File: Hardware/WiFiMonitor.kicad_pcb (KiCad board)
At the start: 2 copper layers, 0 parts

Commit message: Final
Corregi nombres, y agregue el circuito de programación
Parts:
- added BTRTC1: 3.3V, Battery_Holders:Keystone_1058_1x2032-CoinCell, F.Cu at (120.9, 68.8)
- added C1: 2.2u, Capacitors_SMD:C_0603, F.Cu at (111.8, 99.3)
- added C2: 10u, Capacitors_SMD:C_0603, F.Cu at (112.5, 106.6)
- added C3: 4.7u, Capacitors_SMD:C_0603, F.Cu at (103.6, 94.0)
- added COMUN1: NC, PADS:PAD_5x3mm, F.Cu at (150.9, 90.6)
- added COMUN2: TORRETA, PADS:PAD_5x3mm, F.Cu at (142.6, 90.5)
- added D1: LED_ON, LEDs:LED_0603, F.Cu at (103.9, 100.9)
- added D2: LED_CHAR, LEDs:LED_0603, F.Cu at (103.6, 107.7)
- added D3: RB161, Diodes_SMD:D_SOD-123, F.Cu at (122.1, 112.5)
- added D4: RB161, Diodes_SMD:D_SOD-123, F.Cu at (128.9, 87.0)
- added IN1: 0_IN, PADS:PAD_5x3mm, F.Cu at (151.1, 102.9)
- added IN2: 1_IN, PADS:PAD_5x3mm, F.Cu at (142.5, 102.6)
- added IN3: 2_IN, PADS:PAD_5x3mm, F.Cu at (141.1, 96.2)
- added IN4: 3_IN, PADS:PAD_5x3mm, F.Cu at (154.3, 97.0)
- added J3: BATT, Connectors:PINHEAD1-2, F.Cu at (134.0, 112.0)
- added J4: ADAP_ESP, Pin_Headers:Pin_Header_Straight_2x08_Pitch2.54mm, F.Cu at (133.5, 87.0)
- added J5: FTDI, Pin_Headers:Pin_Header_Straight_1x05_Pitch2.54mm, F.Cu at (127.1, 102.5)
- added R1: 2K, Resistors_SMD:R_0603, F.Cu at (114.9, 91.3)
- added R10: 10K, Resistors_SMD:R_0603, F.Cu at (96.4, 106.8)
- added R11: 4.7K, Resistors_SMD:R_0603, F.Cu at (96.9, 112.3)
- added R12: 10K, Resistors_SMD:R_0603, F.Cu at (112.5, 112.5)
- added R13: 4.7K, Resistors_SMD:R_0603, F.Cu at (92.3, 86.4)
- added R14: 10K, Resistors_SMD:R_0603, F.Cu at (91.9, 91.4)
- added R15: 1K, Resistors_SMD:R_0603, F.Cu at (91.6, 96.1)
- added R16: 10K, Resistors_SMD:R_0603, F.Cu at (90.8, 100.7)
- added R17: 1K, Resistors_SMD:R_0603, F.Cu at (90.9, 106.1)
- added R18: 10K, Resistors_SMD:R_0603, F.Cu at (88.4, 112.3)
- added R2: 2K, Resistors_SMD:R_0603, F.Cu at (103.1, 112.8)
- added R3: 2K, Resistors_SMD:R_0603, F.Cu at (96.6, 93.0)
- added R4: 2K, Resistors_SMD:R_0603, F.Cu at (106.9, 87.0)
- added R5: 10K, Resistors_SMD:R_0603, F.Cu at (118.3, 96.4)
- added R6: 10K, Resistors_SMD:R_0603, F.Cu at (109.3, 94.4)
- added R7: 10K, Resistors_SMD:R_0603, F.Cu at (96.7, 99.3)
- added R8: 10K, Resistors_SMD:R_0603, F.Cu at (119.3, 105.1)
- added R9: 10K, Resistors_SMD:R_0603, F.Cu at (99.7, 86.9)
- added U1: 4N25, Housings_DIP:DIP-6_W7.62mm, F.Cu at (142.4, 109.3)
- added U2: 4N25, Housings_DIP:DIP-6_W7.62mm, F.Cu at (155.6, 103.1)
- added U3: 4N25, Housings_DIP:DIP-6_W7.62mm, F.Cu at (156.8, 88.3)
- added U4: 4N25, Housings_DIP:DIP-6_W7.62mm, F.Cu at (141.0, 78.7)
- added U5: MCP73831T-4ADI/OT, MCP73831T-4ADI_OT:SOT95P280X145-5N, F.Cu at (133.7, 82.0)
- added U7: DS3231MZ+, DS3231MZ_:SOIC8_150MIL, F.Cu at (154.9, 82.1)

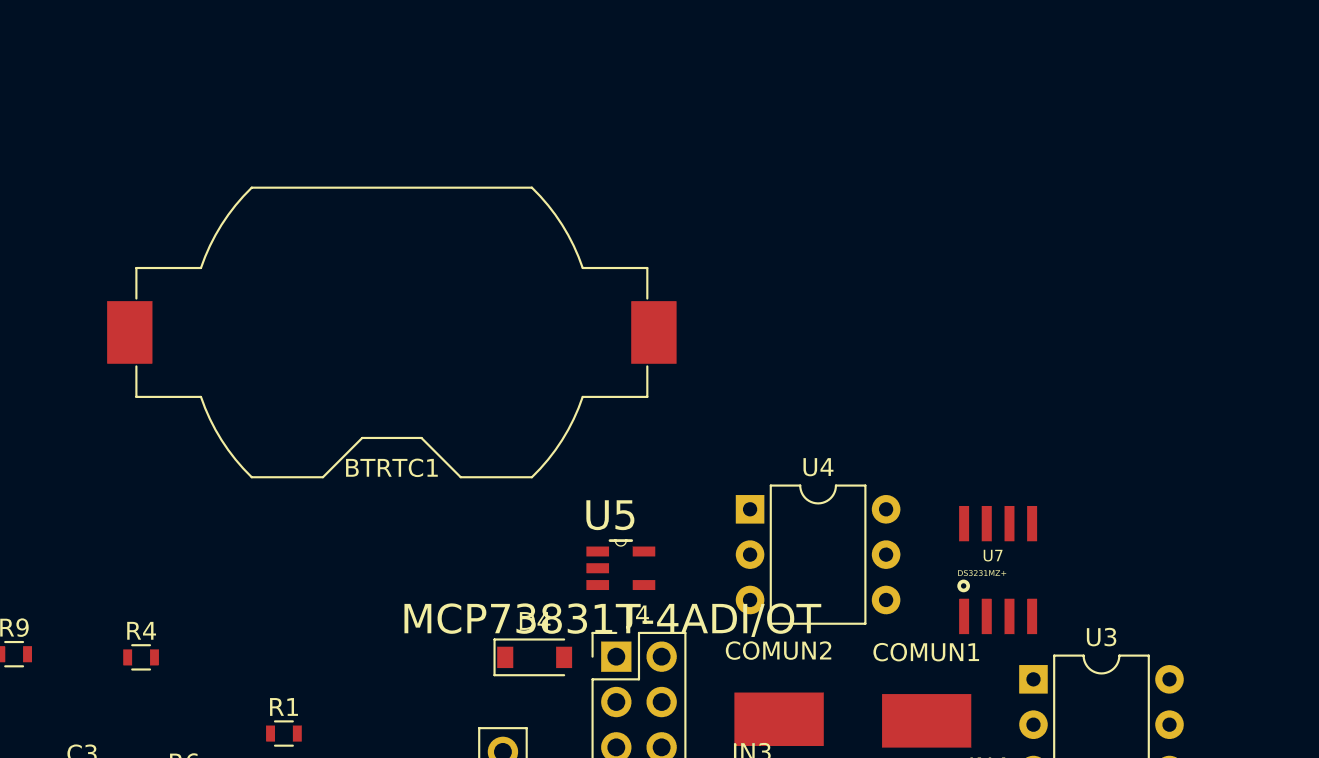
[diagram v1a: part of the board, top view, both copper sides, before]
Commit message: PULL_UP_BOTTON
RESISTENCIAS CORREGIDAS PULL UP DEL RTC Y CAMBIO DE BOTON
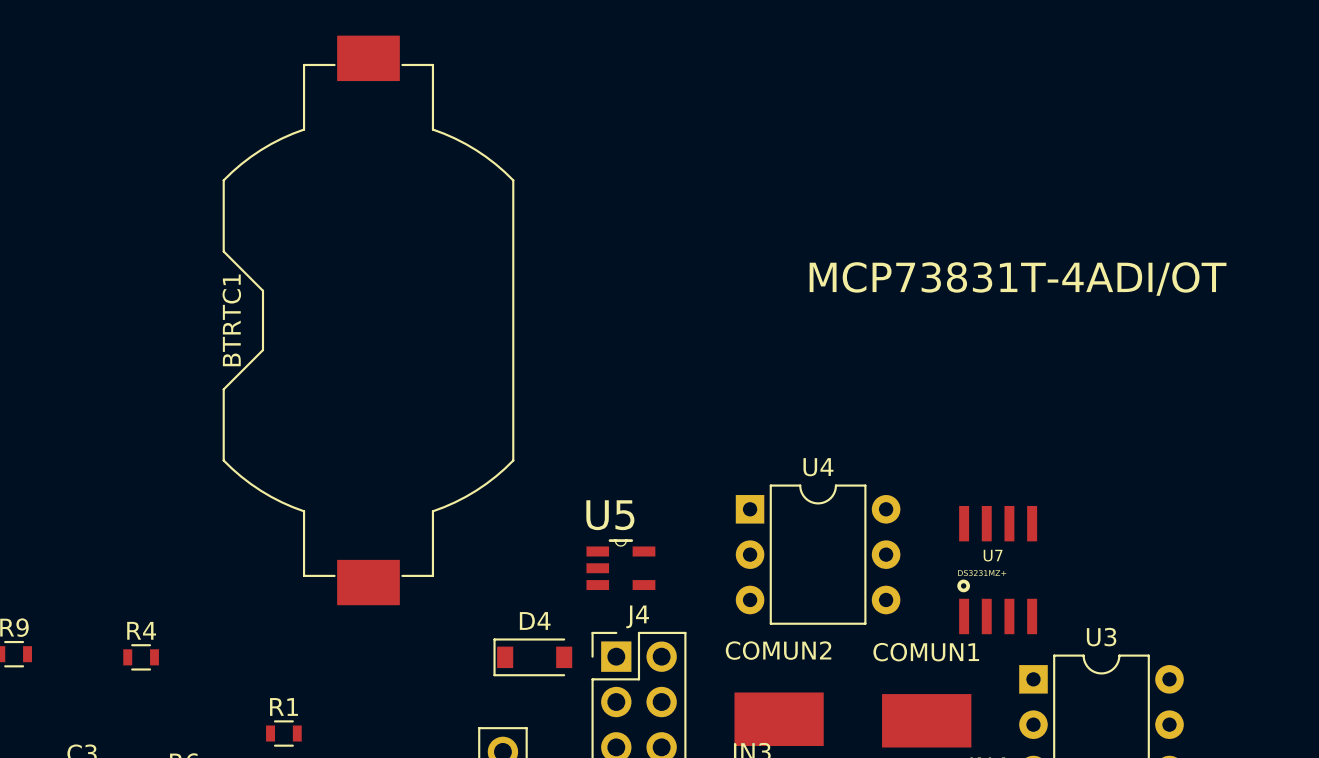
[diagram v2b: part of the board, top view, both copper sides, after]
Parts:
- moved BTRTC1 1.47 mm to (119.6, 68.2), turned to 270 degrees
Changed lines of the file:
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@@
 (kicad_pcb (version 4) (host pcbnew 4.0.7)
   (general
-    (links 71)
-    (no_connects 71)
-    (area 0 0 0 0)
+    (links 81)
+    (no_connects 81)
+    (area 86.714219 51.485899 210.369676 120.581842)
     (thickness 1.6)
     (drawings 2)
@@
   )
   (module Battery_Holders:Keystone_1058_1x2032-CoinCell (layer F.Cu)
-    (at 120.904 68.834)
+    (at 119.5959 68.1609 270)
     (descr http://www.keyelco.com/product-pdf.cfm?p=14028)
     (tags "Keystone type 1058 coin cell retainer")
     (attr smd)
-    (fp_text reference BTRTC1 (at 0 7.62) (layer F.SilkS)
-      (effects (font (size 1 1) (thickness 0.15)))
-    )
-    (fp_text value 3.3V (at 0 -9.398) (layer F.Fab)
+    (fp_text reference BTRTC1 (at 0 7.62 270) (layer F.SilkS)
+      (effects (font (size 1 1) (thickness 0.15)))
+    )
+    (fp_text value 3.3V (at 0 -9.398 270) (layer F.Fab)
       (effects (font (size 1 1) (thickness 0.15)))
     )
@@
     (fp_arc (start 0 0) (end -10.61275 -3.5) (angle 27.4635) (layer F.Fab) (width 0.1))
     (fp_circle (center 0 0) (end 10 0) (layer Dwgs.User) (width 0.15))
-    (pad 1 smd rect (at -14.68 0) (size 2.54 3.51) (layers F.Cu F.Paste F.Mask)
+    (pad 1 smd rect (at -14.68 0 270) (size 2.54 3.51) (layers F.Cu F.Paste F.Mask)
       (net 1 "Net-(BTRTC1-Pad1)"))
-    (pad 2 smd rect (at 14.68 0) (size 2.54 3.51) (layers F.Cu F.Paste F.Mask)
+    (pad 2 smd rect (at 14.68 0 270) (size 2.54 3.51) (layers F.Cu F.Paste F.Mask)
       (net 2 GND))
   )
@@
       (effects (font (size 1.6431 1.6431) (thickness 0.05)))
     )
-    (fp_text value MCP73831T-4ADI/OT (at -0.560846 2.88063) (layer F.SilkS)
+    (fp_text value MCP73831T-4ADI/OT (at 22.1361 -16.2306) (layer F.SilkS)
       (effects (font (size 1.64595 1.64595) (thickness 0.05)))
     )

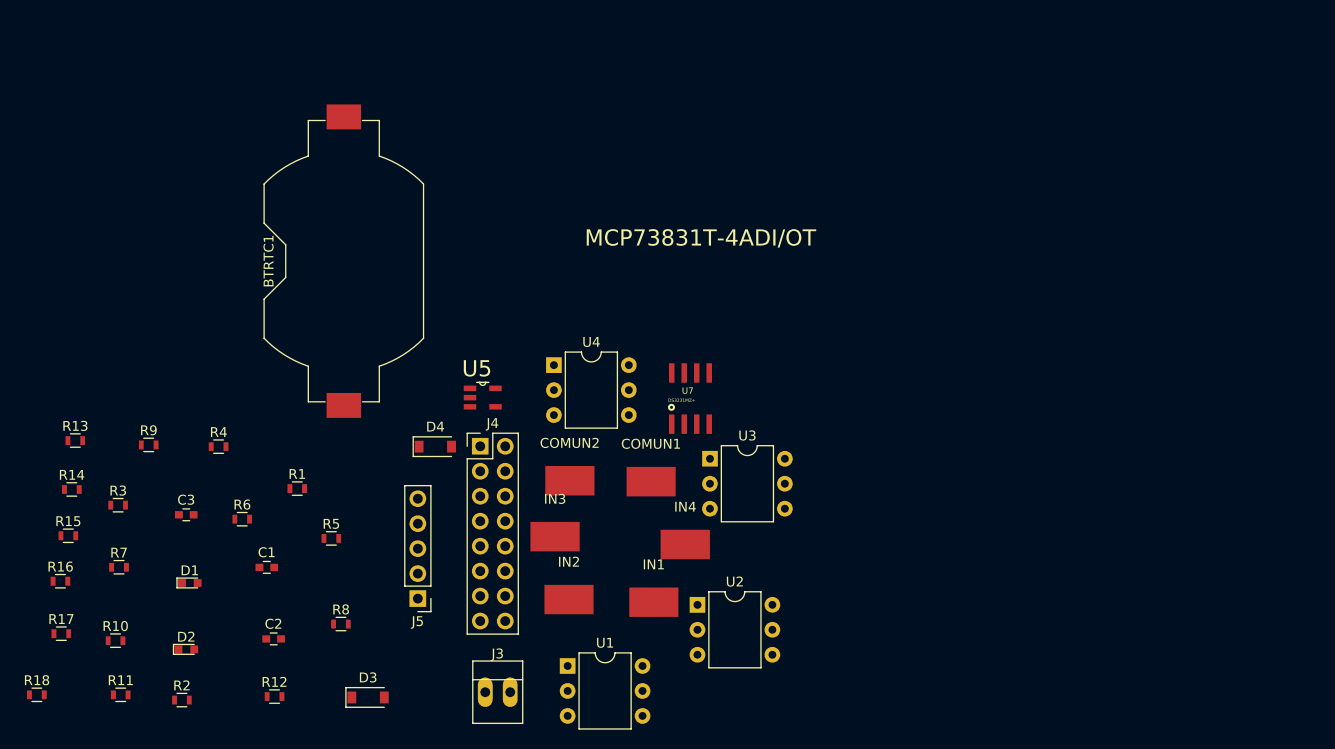
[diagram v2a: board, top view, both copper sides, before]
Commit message: ADAP_MEDIDAS
Adaptador del ESP8266 para programación. Y modificacion del esquematico placa principal para el adaptador.
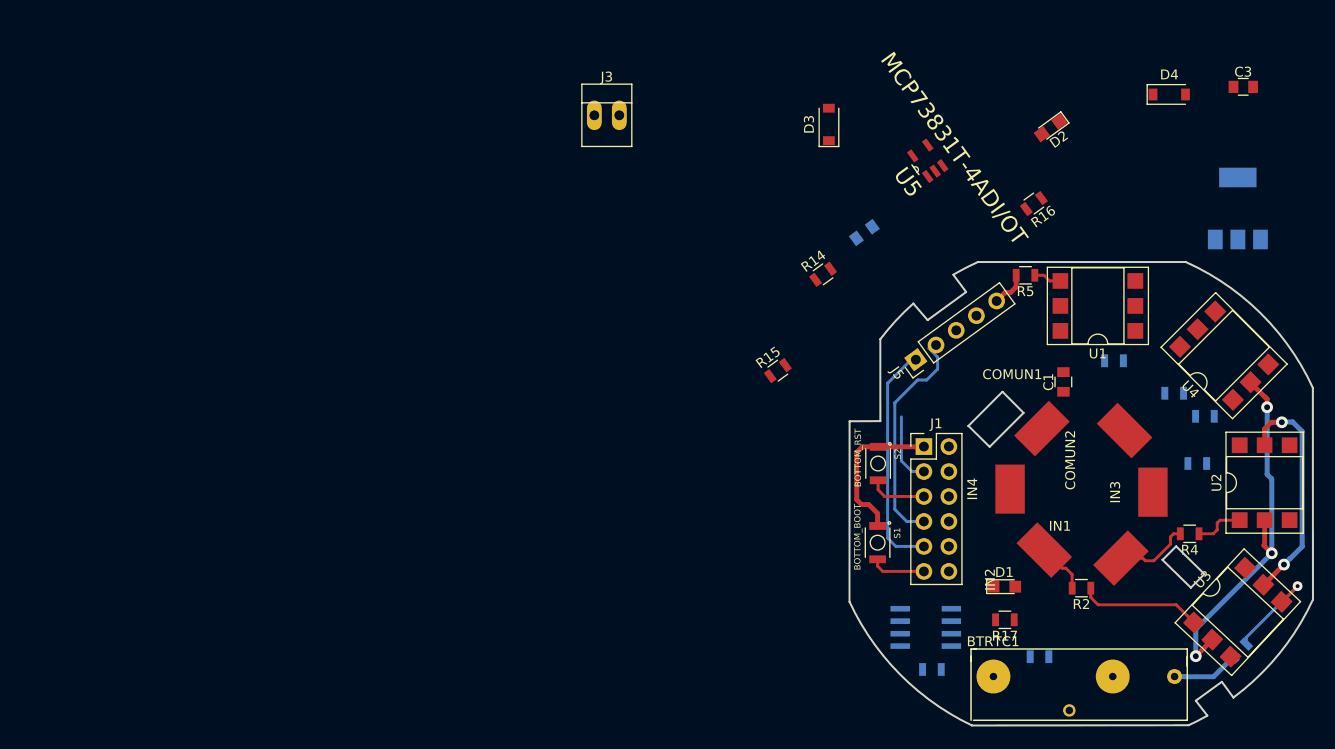
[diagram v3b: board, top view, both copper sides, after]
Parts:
- removed J4: ADAP_ESP, Pin_Headers:Pin_Header_Straight_2x08_Pitch2.54mm
- removed R10, R12, R18, R9: 10K, Resistors_SMD:R_0603
- added J1: ADAP_ESP, Pin_Headers:Pin_Header_Straight_2x06_Pitch2.54mm, F.Cu at (178.6, 87.0)
- added S1: BOTTOM_BOOT, B3U-1000P:SW_B3U-1000P, F.Cu at (173.9, 96.8)
- added S2: BOTTOM_RST, B3U-1000P:SW_B3U-1000P, F.Cu at (173.9, 88.8)
- added U6: AP1117-33, TO_SOT_Packages_SMD:SOT-223-3_TabPin2, B.Cu at (210.6, 62.8)
- BTRTC1: value 3.3V -> 3.3Va; footprint Battery_Holders:Keystone_1058_1x2032-CoinCell -> PADS:Keystone_battery
- C1, C3: footprint Capacitors_SMD:C_0603 -> Capacitors_SMD:C_0805
- C2: footprint Capacitors_SMD:C_0603 -> Capacitors_SMD:C_0805; moved to B.Cu
- COMUN1, COMUN2, IN1, IN2: footprint PADS:PAD_5x3mm -> PADS:Pad_5x3mm_45
- D1, D2: footprint LEDs:LED_0603 -> LEDs:LED_0805
- D3, D4: value RB161 -> NRVB120
- R1, R11, R13, R3, R6, R7, R8: footprint Resistors_SMD:R_0603 -> Resistors_SMD:R_0805; moved to B.Cu
- R14, R15, R16, R17, R2, R4, R5: footprint Resistors_SMD:R_0603 -> Resistors_SMD:R_0805
- U1, U2, U3, U4: footprint Housings_DIP:DIP-6_W7.62mm -> Housings_DIP:DIP-6_W7.62mm_SMDSocket_SmallPads
- U7: moved to B.Cu
- moved C3 116.0 mm to (211.1, 50.4)
- moved R7 114.3 mm to (210.7, 107.8), turned to 45 degrees
- moved R3 108.0 mm to (204.1, 81.6)
- moved R16 106.2 mm to (189.8, 62.3), turned to 216 degrees
- moved D2 102.7 mm to (191.5, 54.6), turned to 216 degrees
- moved R4 99.2 mm to (205.7, 95.9), turned to 180 degrees
- moved R6 97.3 mm to (206.4, 88.8), turned to 180 degrees
- moved R17 96.0 mm to (186.8, 104.7), turned to 180 degrees
- moved R11 93.6 mm to (190.4, 108.4), turned to 180 degrees
- moved R2 92.2 mm to (194.6, 101.4), turned to 180 degrees
- moved R8 90.4 mm to (207.2, 84.0)
- moved R13 90.2 mm to (179.4, 109.7), turned to 180 degrees
- moved BTRTC1 86.8 mm to (193.4, 113.9), turned to 0 degrees
- moved R1 84.1 mm to (197.9, 78.3)
- moved C1 83.2 mm to (192.8, 80.5), turned to 90 degrees
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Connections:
- net /VCC renamed VCC
- R11 pad 1: Net-(R11-Pad1) -> /SCL
- R11 pad 2: /SCL -> +3V3
- R13 pad 2: Net-(R13-Pad2) -> +3V3
- U7 pad 7: Net-(R13-Pad2) -> /SDA
- U7 pad 8: Net-(R11-Pad1) -> /SCL
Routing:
- net GNDA: track 0.00 -> 38.1 mm, vias 0 -> 3
- net GND: track 0.00 -> 26.4 mm
- net +3V3: track 0.00 -> 23.4 mm, vias 0 -> 2
- net /TX: track 0.00 -> 22.8 mm
- net /RX: track 0.00 -> 22.6 mm
- net Net-(R2-Pad1): track 0.00 -> 12.5 mm
- net /D1: track 0.00 -> 10.3 mm, vias 0 -> 1
- net Net-(IN1-Pad1): track 0.00 -> 7.74 mm
- net /D0: track 0.00 -> 7.22 mm
- net /RST: track 0.00 -> 5.92 mm
- net /GPIO0: track 0.00 -> 5.63 mm
- net Net-(IN2-Pad1): track 0.00 -> 5.25 mm
- net Net-(R4-Pad1): track 0.00 -> 5.12 mm
- net /D2: track 0.00 -> 2.84 mm
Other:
- board outline added: 47.2 x 47.2 mm
- net class Default: trace_width 0.25 -> 0.3; via_dia 0.6 -> 1
- net class SOURCE added: clearance 0.2, trace_width 0.5, via_dia 1.2, via_drill 0.6

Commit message: PCBS_Adap_mon
Correxión del RX y TX del adaptador, PCB monitor doble capa.
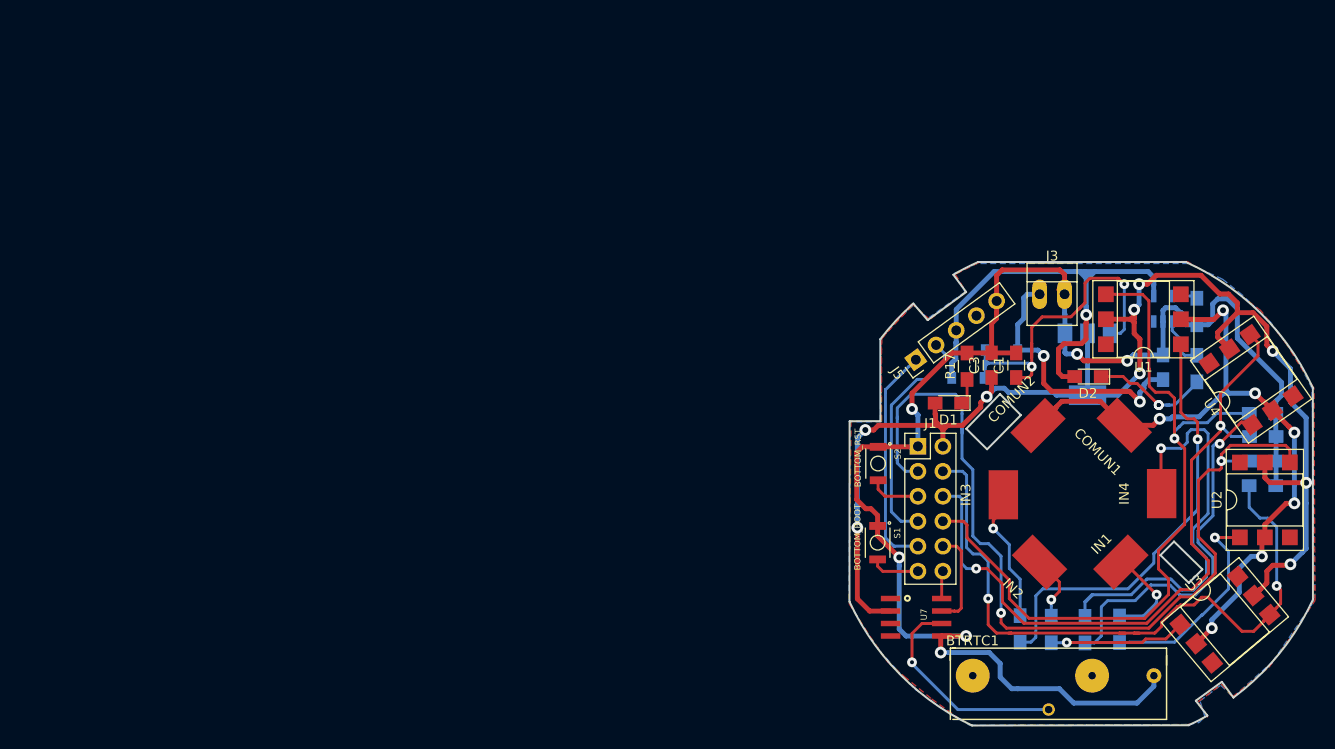
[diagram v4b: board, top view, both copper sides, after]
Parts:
- removed R11, R13: 4.7K, Resistors_SMD:R_0805
- removed R16: 10K, Resistors_SMD:R_0805
- C1, C2, C3: footprint Capacitors_SMD:C_0805 -> Capacitors_SMD:C_0805_HandSoldering
- COMUN1, COMUN2, IN1, IN2: footprint PADS:Pad_5x3mm_45 -> PADS:PAD_5x3mm
- D1, D2: footprint LEDs:LED_0805 -> LEDs:LED_0805_HandSoldering
- D3, D4, U5: moved to B.Cu
- R1, R17, R3, R6, R7, R8: footprint Resistors_SMD:R_0805 -> Resistors_SMD:R_0805_HandSoldering
- R14, R15, R2, R4, R5: footprint Resistors_SMD:R_0805 -> Resistors_SMD:R_0805_HandSoldering; moved to B.Cu
- U7: moved to F.Cu
- moved J3 48.8 mm to (190.4, 71.5)
- moved R15 42.6 mm to (206.4, 79.1), turned to 270 degrees
- moved R14 38.2 mm to (206.4, 73.3), turned to 90 degrees
- moved C3 38.2 mm to (185.5, 78.8), turned to 90 degrees
- moved D4 35.4 mm to (183.1, 80.0), turned to 180 degrees
- moved C2 33.3 mm to (202.9, 79.0), turned to 90 degrees
- moved D3 28.9 mm to (186.5, 77.2), turned to 0 degrees
- moved R1 28.9 mm to (188.4, 105.6), turned to 90 degrees
- moved U5 28.3 mm to (202.9, 73.0), turned to 90 degrees
- moved R5 27.9 mm to (213.1, 83.7), turned to 0 degrees
- moved R17 26.1 mm to (183.0, 78.8), turned to 90 degrees
- moved R3 25.7 mm to (195.0, 105.7), turned to 90 degrees
- moved D2 25.6 mm to (195.3, 79.9), turned to 180 degrees
- moved U6 22.0 mm to (195.3, 78.7), turned to 270 degrees
- moved D1 19.5 mm to (181.1, 82.6), turned to 180 degrees
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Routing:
- net GND: track 26.4 -> 152.6 mm, vias 0 -> 6
- net +3V3: track 23.4 -> 142.2 mm, vias 2 -> 9
- net /D0: track 7.22 -> 91.5 mm, vias 0 -> 2
- net /D2: track 2.84 -> 78.1 mm, vias 0 -> 1
- net /D3: track 0.00 -> 71.1 mm, vias 0 -> 2
- net /D1: track 10.3 -> 68.8 mm, vias 1 -> 2
- net VCC: track 0.00 -> 48.8 mm, vias 0 -> 1
- net Net-(R1-Pad1): track 0.00 -> 45.2 mm, vias 0 -> 1
- net Net-(IN4-Pad1): track 0.00 -> 43.6 mm, vias 0 -> 1
- net Net-(R3-Pad1): track 0.00 -> 37.8 mm, vias 0 -> 1
- net Net-(C1-Pad1): track 0.00 -> 36.5 mm, vias 0 -> 2
- net GNDA: track 38.1 -> 72.6 mm, vias 3 -> 7
- net /BAT: track 0.00 -> 28.1 mm, vias 0 -> 2
- net Net-(BTRTC1-Pad1): track 0.00 -> 22.3 mm, vias 0 -> 1
- net Net-(R4-Pad1): track 5.12 -> 21.8 mm, vias 0 -> 1
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- added copper zone on B.Cu, net GND
- added copper zone on F.Cu, net GND
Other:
- outline, holes or cut-outs redrawn

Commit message: Tracks fix
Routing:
- net Net-(IN4-Pad1): track 43.6 -> 35.6 mm
- net GNDA: track 72.6 -> 77.6 mm, vias 7 -> 6
- net +3V3: track 142.2 -> 146.7 mm
- net Net-(R2-Pad1): track 13.9 -> 17.3 mm
- net Net-(R3-Pad1): track 37.8 -> 36.4 mm
- net /D0: track 91.5 -> 90.2 mm
- net /D3: track 71.1 -> 72.4 mm
- net /D2: track 78.1 -> 77.3 mm
- net /D1: track 68.8 -> 69.6 mm

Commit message: PCB_PISTAS
Reacomodo de pistas
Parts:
- moved R6 3.31 mm to (211.7, 91.5)
- moved R8 3.31 mm to (211.7, 89.0)
- moved R7 3.22 mm to (211.7, 93.9)
- moved R5 3.18 mm to (211.7, 86.5)
- moved R14 2.24 mm to (204.9, 71.6), turned to 0 degrees
- moved U5 1.74 mm to (202.9, 74.8)
- moved R15 0.98 mm to (205.6, 79.7)
- moved C2 0.51 mm to (202.9, 79.5)
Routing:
- net GND: track 152.1 -> 155.7 mm
- net /D0: track 90.2 -> 86.9 mm
- net GNDA: track 77.6 -> 80.7 mm, vias 6 -> 8
- net +3V3: track 146.7 -> 144.2 mm
- net VCC: track 48.8 -> 50.6 mm
- net Net-(R15-Pad1): track 5.21 -> 3.76 mm
- net /D1: track 69.6 -> 68.2 mm
- net Net-(R14-Pad2): track 2.60 -> 3.96 mm
- net Net-(R3-Pad1): track 36.4 -> 35.4 mm
- net Net-(R1-Pad1): track 45.2 -> 44.2 mm
- net Net-(IN4-Pad1): track 35.6 -> 34.8 mm
- net /D2: track 77.3 -> 76.6 mm
- net /D3: track 72.4 -> 72.9 mm
